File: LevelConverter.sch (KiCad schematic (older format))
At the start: 3 parts, among them Q3 BSS138

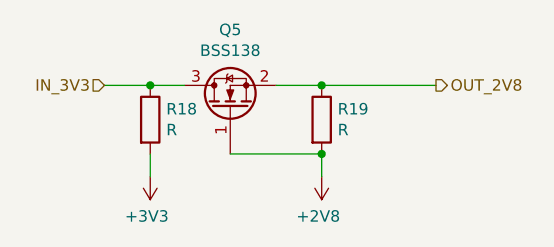
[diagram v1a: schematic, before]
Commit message: Added IC for level translation with ultrasonic sensors
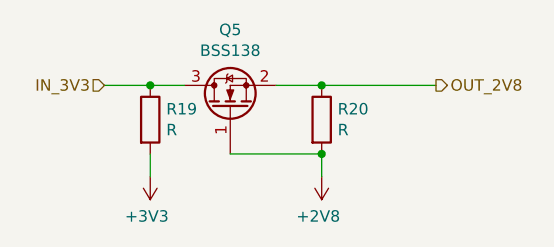
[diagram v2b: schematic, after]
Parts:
- R19: renamed from R14; footprint (none) -> Resistor_SMD:R_0805_2012Metric_Pad1.15x1.40mm_HandSolder
- R20: renamed from R15; footprint (none) -> Resistor_SMD:R_0805_2012Metric_Pad1.15x1.40mm_HandSolder
- renumbered Q3 to Q5
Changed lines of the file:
@@
 $Descr A4 11693 8268
 encoding utf-8
-Sheet 18 19
+Sheet 17 19
 Title ""
 Date ""
@@
 AR Path="/5BBFB811/5BBEDD8D" Ref="Q?"  Part="1"
 AR Path="/5BBFB816/5BBEDD8D" Ref="Q?"  Part="1"
-AR Path="/5BBEDBC7/5BBEDD8D" Ref="Q3"  Part="1"
+AR Path="/5BBEDBC7/5BBEDD8D" Ref="Q5"  Part="1"
 AR Path="/5BBEFA1A/5BBEDD8D" Ref="Q4"  Part="1"
-AR Path="/5BBEFA89/5BBEDD8D" Ref="Q5"  Part="1"
+AR Path="/5BBEFA89/5BBEDD8D" Ref="Q3"  Part="1"
 F 0 "Q5" V 4343 3100 50  0000 C CNN
 F 1 "BSS138" V 4252 3100 50  0000 C CNN
@@
 AR Path="/5BBFB811/5BBEDD94" Ref="R?"  Part="1"
 AR Path="/5BBFB816/5BBEDD94" Ref="R?"  Part="1"
-AR Path="/5BBEDBC7/5BBEDD94" Ref="R15"  Part="1"
-AR Path="/5BBEFA1A/5BBEDD94" Ref="R17"  Part="1"
-AR Path="/5BBEFA89/5BBEDD94" Ref="R19"  Part="1"
-F 0 "R19" H 4470 3196 50  0000 L CNN
+AR Path="/5BBEDBC7/5BBEDD94" Ref="R20"  Part="1"
+AR Path="/5BBEFA1A/5BBEDD94" Ref="R18"  Part="1"
+AR Path="/5BBEFA89/5BBEDD94" Ref="R14"  Part="1"
+F 0 "R20" H 4470 3196 50  0000 L CNN
 F 1 "R" H 4470 3105 50  0000 L CNN
-F 2 "" V 4330 3150 50  0001 C CNN
+F 2 "Resistor_SMD:R_0805_2012Metric_Pad1.15x1.40mm_HandSolder" V 4330 3150 50  0001 C CNN
 F 3 "~" H 4400 3150 50  0001 C CNN
 	1    4400 3150
@@
 AR Path="/5BBFB811/5BBEDD9D" Ref="#PWR?"  Part="1"
 AR Path="/5BBFB816/5BBEDD9D" Ref="#PWR?"  Part="1"
-AR Path="/5BBEDBC7/5BBEDD9D" Ref="#PWR063"  Part="1"
-AR Path="/5BBEFA1A/5BBEDD9D" Ref="#PWR065"  Part="1"
-AR Path="/5BBEFA89/5BBEDD9D" Ref="#PWR067"  Part="1"
-F 0 "#PWR067" H 4400 3250 50  0001 C CNN
+AR Path="/5BBEDBC7/5BBEDD9D" Ref="#PWR073"  Part="1"
+AR Path="/5BBEFA1A/5BBEDD9D" Ref="#PWR071"  Part="1"
+AR Path="/5BBEFA89/5BBEDD9D" Ref="#PWR057"  Part="1"
+F 0 "#PWR073" H 4400 3250 50  0001 C CNN
 F 1 "+2V8" H 4415 3573 50  0000 C CNN
 F 2 "" H 4400 3400 50  0001 C CNN
@@
 AR Path="/5BBFB811/5BBEDDA3" Ref="R?"  Part="1"
 AR Path="/5BBFB816/5BBEDDA3" Ref="R?"  Part="1"
-AR Path="/5BBEDBC7/5BBEDDA3" Ref="R14"  Part="1"
-AR Path="/5BBEFA1A/5BBEDDA3" Ref="R16"  Part="1"
-AR Path="/5BBEFA89/5BBEDDA3" Ref="R18"  Part="1"
-F 0 "R18" H 3720 3196 50  0000 L CNN
+AR Path="/5BBEDBC7/5BBEDDA3" Ref="R19"  Part="1"
+AR Path="/5BBEFA1A/5BBEDDA3" Ref="R17"  Part="1"
+AR Path="/5BBEFA89/5BBEDDA3" Ref="R13"  Part="1"
+F 0 "R19" H 3720 3196 50  0000 L CNN
 F 1 "R" H 3720 3105 50  0000 L CNN
-F 2 "" V 3580 3150 50  0001 C CNN
+F 2 "Resistor_SMD:R_0805_2012Metric_Pad1.15x1.40mm_HandSolder" V 3580 3150 50  0001 C CNN
 F 3 "~" H 3650 3150 50  0001 C CNN
 	1    3650 3150
@@
 AR Path="/5BBFB811/5BBEDDAD" Ref="#PWR?"  Part="1"
 AR Path="/5BBFB816/5BBEDDAD" Ref="#PWR?"  Part="1"
-AR Path="/5BBEDBC7/5BBEDDAD" Ref="#PWR062"  Part="1"
-AR Path="/5BBEFA1A/5BBEDDAD" Ref="#PWR064"  Part="1"
-AR Path="/5BBEFA89/5BBEDDAD" Ref="#PWR066"  Part="1"
-F 0 "#PWR066" H 3650 3250 50  0001 C CNN
+AR Path="/5BBEDBC7/5BBEDDAD" Ref="#PWR072"  Part="1"
+AR Path="/5BBEFA1A/5BBEDDAD" Ref="#PWR070"  Part="1"
+AR Path="/5BBEFA89/5BBEDDAD" Ref="#PWR056"  Part="1"
+F 0 "#PWR072" H 3650 3250 50  0001 C CNN
 F 1 "+3V3" H 3665 3573 50  0000 C CNN
 F 2 "" H 3650 3400 50  0001 C CNN

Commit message: Footprint association
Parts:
- Q5: footprint Package_TO_SOT_SMD:SOT-23 -> Package_TO_SOT_SMD:SOT-23_Handsoldering
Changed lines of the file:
@@
 F 0 "Q5" V 4343 3100 50  0000 C CNN
 F 1 "BSS138" V 4252 3100 50  0000 C CNN
-F 2 "Package_TO_SOT_SMD:SOT-23" H 4200 3025 50  0001 L CIN
+F 2 "Package_TO_SOT_SMD:SOT-23_Handsoldering" H 4200 3025 50  0001 L CIN
 F 3 "https://www.fairchildsemi.com/datasheets/BS/BSS138.pdf" H 4000 3100 50  0001 L CNN
 	1    4000 3100

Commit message: Added RS refs
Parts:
- Q5: RS (none) -> 545-2529
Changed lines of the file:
@@
 F 2 "Package_TO_SOT_SMD:SOT-23_Handsoldering" H 4200 3025 50  0001 L CIN
 F 3 "https://www.fairchildsemi.com/datasheets/BS/BSS138.pdf" H 4000 3100 50  0001 L CNN
+F 4 "545-2529" H 0   0   50  0001 C CNN "RS"
 	1    4000 3100
 	0    -1   -1   0
